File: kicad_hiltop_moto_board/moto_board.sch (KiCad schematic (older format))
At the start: 45 parts, among them J1 Conn_01x04, J2 Conn_01x03, J3 Conn_03x32_DIN41612, J4 Conn_01x03, J5 Conn_02x05_Top_Bottom, U2 LD1117S33TR_SOT223, U3 AT25DN512CSSHF-B

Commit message: Unused pind removed from moto board
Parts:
- C10, C11, C12: symbol Motor_Control_Board-rescue:C-device-Sensi_Board-rescue -> moto_board-rescue:C-device-Sensi_Board-rescue-Motor_Control_Board-rescue
- C13: symbol Motor_Control_Board-rescue:CP-device-Sensi_Board-rescue -> moto_board-rescue:CP-device-Sensi_Board-rescue-Motor_Control_Board-rescue
- D32: symbol Motor_Control_Board-rescue:D-device-Sensi_Board-rescue -> moto_board-rescue:D-device-Sensi_Board-rescue-Motor_Control_Board-rescue
- J3: symbol Motor_Control_Board-rescue:Conn_03x32_DIN41612-Devtank-Sensi_Board-rescue -> moto_board-rescue:Conn_03x32_DIN41612-Devtank-Sensi_Board-rescue-Motor_Control_Board-rescue
- JP1: symbol Motor_Control_Board-rescue:Jumper_NC_Dual-device-Sensi_Board-rescue -> moto_board-rescue:Jumper_NC_Dual-device-Sensi_Board-rescue-Motor_Control_Board-rescue
- R14, R15, R16, R17: symbol Motor_Control_Board-rescue:R-device-Sensi_Board-rescue -> moto_board-rescue:R-device-Sensi_Board-rescue-Motor_Control_Board-rescue
- TP101, TP102, TP103, TP104, TP105, TP2, TP31, TP32, TP33, TP34, TP35, TP36: symbol Motor_Control_Board-rescue:Test_Point-Connector-Sensi_Board-rescue -> moto_board-rescue:Test_Point-Connector-Sensi_Board-rescue-Motor_Control_Board-rescue
- U2: symbol Motor_Control_Board-rescue:LD1117S33TR_SOT223-regul-Sensi_Board-rescue -> moto_board-rescue:LD1117S33TR_SOT223-regul-Sensi_Board-rescue-Motor_Control_Board-rescue
- U3: symbol Motor_Control_Board-rescue:AT25_EEPROM-memory-Sensi_Board-rescue -> moto_board-rescue:AT25_EEPROM-memory-Sensi_Board-rescue-Motor_Control_Board-rescue
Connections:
- net labels removed: ADC1, ADC10, ADC11, ADC12, ADC13, ADC2, ADC3, ADC4, ADC5, ADC6, ADC7, ADC8, ADC9
- wire segments 285 -> 272
- no-connect marks 88 -> 64
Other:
- note added: "Direct PWM"
- note added: "PWM through SPI\n"

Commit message: Started on moto board layout
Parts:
- removed J2, J4: Conn_01x03, symbol Connector:Conn_01x03
- added J2, J4: Conn_01x04, Devtank_PCB_Lib:Molex2x06, symbol Connector:Conn_01x04
- added TP1, TP10, TP11, TP12, TP13, TP14, TP15, TP16, TP23, TP3, TP4, TP5, TP6, TP7, TP8, TP9: Test_Point, TestPoint:TestPoint_THTPad_D1.0mm_Drill0.5mm, symbol moto_board-rescue:Test_Point-Connector-Sensi_Board-rescue-Motor_Control_Board-r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
- J1: footprint (none) -> Connector_TE-Connectivity:TE_MATE-N-LOK_350211-1_1x04_P5.08mm_Vertical
- J5: footprint (none) -> Connector_PinHeader_2.54mm:PinHeader_2x05_P2.54mm_Vertical
- R1, R13: footprint (none) -> Resistor_SMD:R_0805_2012Metric
- R10, R11, R12, R2, R3, R4, R5, R6, R7, R8, R9: footprint (none) -> Resistor_SMD:R_0603_1608Metric
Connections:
- net 12V_EXT: now also TP12.1
- net AOUT1: now also J4.1 (Pin_1), TP13.1
- net AOUT2: now also J4.2 (Pin_2), TP14.1
- net BOUT1: now also J2.1 (Pin_1), TP15.1
- net BOUT2: now also J2.2 (Pin_2), TP16.1
- net GND: now also J2.3 (Pin_3), J4.3 (Pin_3)
- net motor_AIN1 renamed M_AIN1
- net M_AIN1: now also TP4.1
- net motor_AIN2 renamed M_AIN2
- net M_AIN2: now also TP5.1
- net motor_BIN1 renamed M_BIN1
- net M_BIN1: now also TP6.1
- net motor_BIN2 renamed M_BIN2
- net M_BIN2: now also TP7.1
- net motor_DATO renamed M_SDATO
- net M_SDATO: now also TP11.1
- net motor_FAULTn renamed M_FAULTn
- net M_FAULTn: now also TP23.1
- net motor_RESET renamed M_RESET
- net M_RESET: now also TP3.1
- net motor_SCLK renamed M_SCLK
- net M_SCLK: now also TP8.1
- net motor_SCS renamed M_SCS
- net M_SCS: now also TP10.1
- net motor_SDATI renamed M_SDATI
- net M_SDATI: now also TP9.1
- net motor_SLEEPn renamed M_SLEEPn
- net M_SLEEPn: now also TP1.1
- no-connect marks 64 -> 66

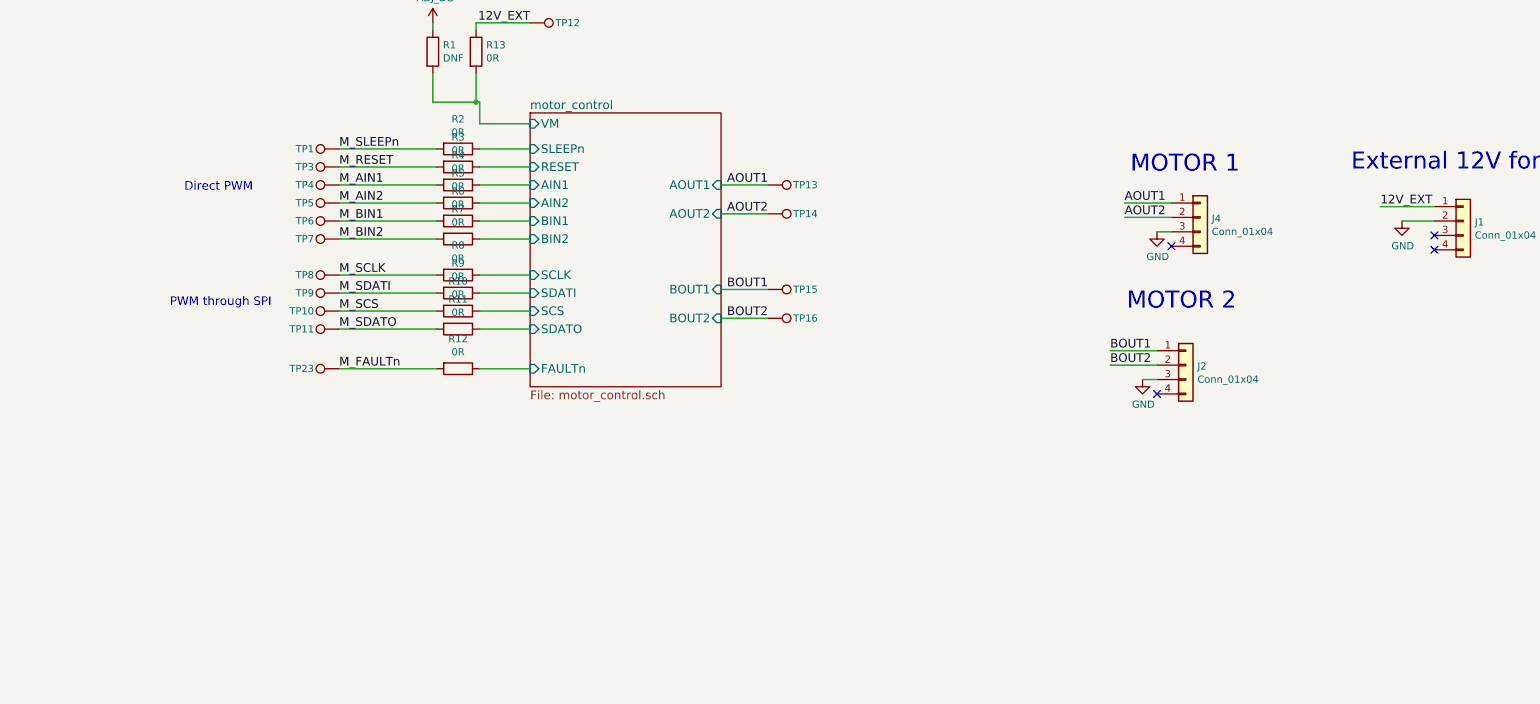
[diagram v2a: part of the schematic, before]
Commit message: Rough layout of moto board
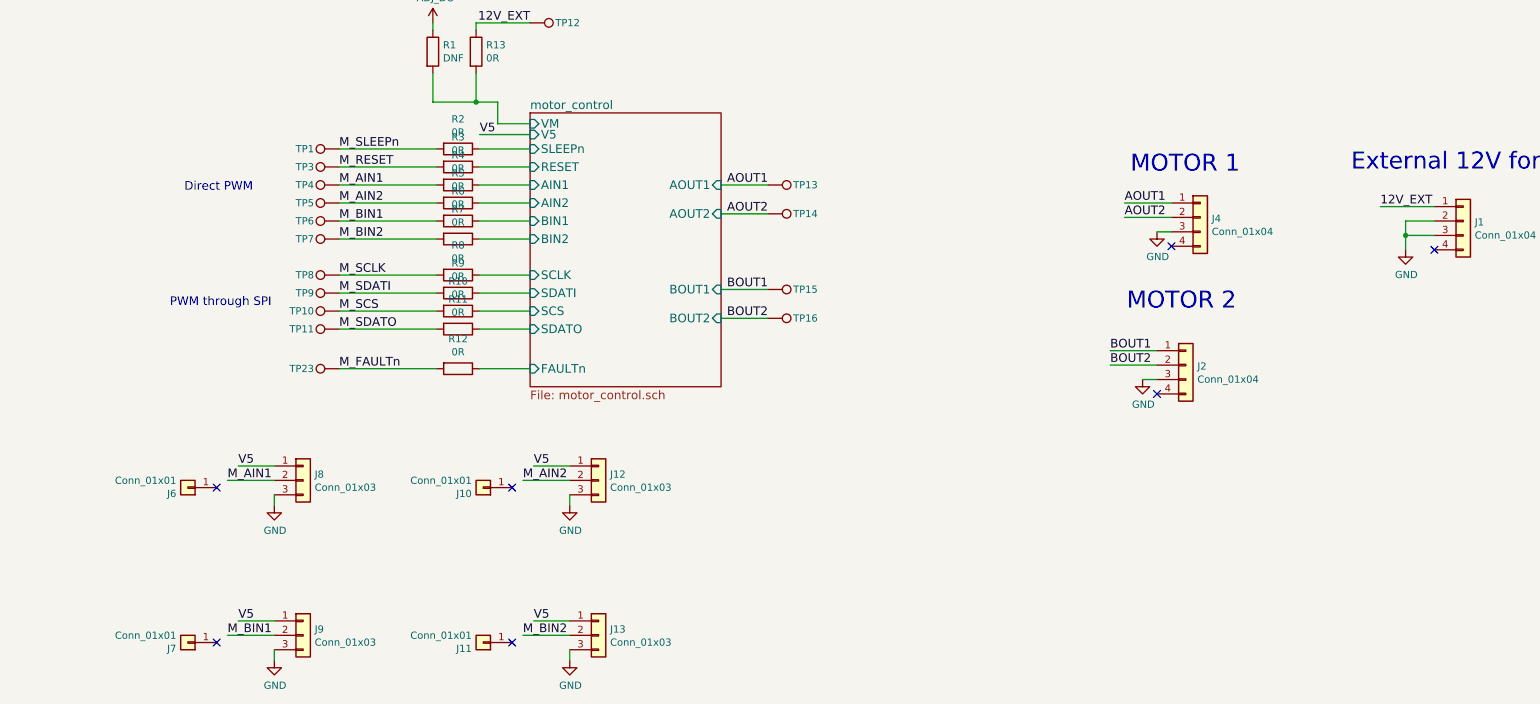
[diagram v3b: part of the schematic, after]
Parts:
- added J10, J11, J6, J7: Conn_01x01, Connector_PinHeader_2.54mm:PinHeader_1x01_P2.54mm_Vertical, symbol Connector:Conn_01x01
- added J12, J13, J8, J9: Conn_01x03, Connector_PinHeader_2.54mm:PinHeader_1x03_P2.54mm_Vertical, symbol Connector:Conn_01x03
- J2, J4: footprint Devtank_PCB_Lib:Molex2x06 -> Connector_Molex:Molex_Nano-Fit_105309-xx04_1x04_P2.50mm_Vertical
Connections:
- net GND: now also J1.3 (Pin_3), J12.3 (Pin_3), J13.3 (Pin_3), J8.3 (Pin_3), J9.3 (Pin_3)
- net M_AIN1: now also J8.2 (Pin_2)
- net M_AIN2: now also J12.2 (Pin_2)
- net M_BIN1: now also J9.2 (Pin_2)
- net M_BIN2: now also J13.2 (Pin_2)
- new net V5: J12.1 (Pin_1), J13.1 (Pin_1), J8.1 (Pin_1), J9.1 (Pin_1)
- no-connect marks 66 -> 69
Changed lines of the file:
@@
 F16 "BOUT2" I R 9025 9800 60
 F17 "VM" I L 7700 8450 60
+F18 "V5" I L 7700 8525 60
 $EndSheet
 Wire Wire Line
@@
 	7325 7800 7325 7750
 Wire Wire Line
-	7700 8450 7350 8450
-Wire Wire Line
-	7350 8450 7350 8300
+	7700 8450 7475 8450
+Wire Wire Line
+	7475 8450 7475 8300
 Wire Wire Line
 	7025 8300 7025 8100
@@
 Connection ~ 7325 8300
 Wire Wire Line
-	7325 8300 7350 8300
+	7325 8300 7475 8300
 Text Label 7700 7750 2    60   ~ 0
 12V_EXT
@@
 L power:GND #PWR04
 U 1 1 61485EFB
-P 13750 9125
-F 0 "#PWR04" H 13750 8875 50  0001 C CNN
-F 1 "GND" H 13755 8952 50  0000 C CNN
-F 2 "" H 13750 9125 50  0001 C CNN
-F 3 "" H 13750 9125 50  0001 C CNN
-	1    13750 9125
-	1    0    0    -1
-$EndComp
-NoConn ~ 13975 9225
+P 13775 9325
+F 0 "#PWR04" H 13775 9075 50  0001 C CNN
+F 1 "GND" H 13780 9152 50  0000 C CNN
+F 2 "" H 13775 9325 50  0001 C CNN
+F 3 "" H 13775 9325 50  0001 C CNN
+	1    13775 9325
+	1    0    0    -1
+$EndComp
 NoConn ~ 13975 9325
-Wire Wire Line
-	13750 9125 13975 9125
 Text Notes 15250 8975 2    118  ~ 0
 External 12V for motor\n\n
@@
 F 0 "J4" H 12430 9092 50  0000 L CNN
 F 1 "Conn_01x04" H 12430 9001 50  0000 L CNN
-F 2 "Devtank_PCB_Lib:Molex2x06" H 12350 9100 50  0001 C CNN
+F 2 "Connector_Molex:Molex_Nano-Fit_105309-xx04_1x04_P2.50mm_Vertical" H 12350 9100 50  0001 C CNN
 F 3 "~" H 12350 9100 50  0001 C CNN
 	1    12350 9100
@@
 F 0 "J2" H 12330 10117 50  0000 L CNN
 F 1 "Conn_01x04" H 12330 10026 50  0000 L CNN
-F 2 "Devtank_PCB_Lib:Molex2x06" H 12250 10125 50  0001 C CNN
+F 2 "Connector_Molex:Molex_Nano-Fit_105309-xx04_1x04_P2.50mm_Vertical" H 12250 10125 50  0001 C CNN
 F 3 "~" H 12250 10125 50  0001 C CNN
 	1    12250 10125
@@
 	0    -1   -1   0
 $EndComp
+$Comp
+L Connector:Conn_01x01 J6
+U 1 1 5DCD017F
+P 5325 10975
+F 0 "J6" H 5405 11017 50  0000 L CNN
+F 1 "Conn_01x01" H 5405 10926 50  0000 L CNN
+F 2 "Connector_PinHeader_2.54mm:PinHeader_1x01_P2.54mm_Vertical" H 5325 10975 50  0001 C CNN
+F 3 "~" H 5325 10975 50  0001 C CNN
+	1    5325 10975
+	-1   0    0    1
+$EndComp
+Wire Wire Line
+	5925 11025 5925 11100
+Wire Wire Line
+	5925 10825 5675 10825
+Wire Wire Line
+	7700 8525 7350 8525
+Text Label 7350 8525 0    60   ~ 0
+V5
+Text Label 5675 10825 0    60   ~ 0
+V5
+NoConn ~ 5525 10975
+$Comp
+L power:GND #PWR0108
+U 1 1 5DEBCBBF
+P 5925 11100
+F 0 "#PWR0108" H 5925 10850 50  0001 C CNN
+F 1 "GND" H 5930 10927 50  0000 C CNN
+F 2 "" H 5925 11100 50  0001 C CNN
+F 3 "" H 5925 11100 50  0001 C CNN
+	1    5925 11100
+	1    0    0    -1
+$EndComp
+Text Label 5600 10925 0    60   ~ 0
+M_AIN1
+Wire Wire Line
+	5600 10925 5925 10925
+$Comp
+L Connector:Conn_01x03 J8
+U 1 1 5DFB262E
+P 6125 10925
+F 0 "J8" H 6205 10967 50  0000 L CNN
+F 1 "Conn_01x03" H 6205 10876 50  0000 L CNN
+F 2 "Connector_PinHeader_2.54mm:PinHeader_1x03_P2.54mm_Vertical" H 6125 10925 50  0001 C CNN
+F 3 "~" H 6125 10925 50  0001 C CNN
+	1    6125 10925
+	1    0    0    -1
+$EndComp
+$Comp
+L Connector:Conn_01x01 J10
+U 1 1 5E06E1C9
+P 7375 10975
+F 0 "J10" H 7455 11017 50  0000 L CNN
+F 1 "Conn_01x01" H 7455 10926 50  0000 L CNN
+F 2 "Connector_PinHeader_2.54mm:PinHeader_1x01_P2.54mm_Vertical" H 7375 10975 50  0001 C CNN
+F 3 "~" H 7375 10975 50  0001 C CNN
+	1    7375 10975
+	-1   0    0    1
+$EndComp
+Wire Wire Line
+	7975 11025 7975 11100
+Wire Wire Line
+	7975 10825 7725 10825
+Text Label 7725 10825 0    60   ~ 0
+V5
+NoConn ~ 7575 10975
+$Comp
+L power:GND #PWR0109
+U 1 1 5E06E1D3
+P 7975 11100
+F 0 "#PWR0109" H 7975 10850 50  0001 C CNN
+F 1 "GND" H 7980 10927 50  0000 C CNN
+F 2 "" H 7975 11100 50  0001 C CNN
+F 3 "" H 7975 11100 50  0001 C CNN
+	1    7975 11100
+	1    0    0    -1
+$EndComp
+Text Label 7650 10925 0    60   ~ 0
+M_AIN2
+Wire Wire Line
+	7650 10925 7975 10925
+$Comp
+L Connector:Conn_01x03 J12
+U 1 1 5E06E1DB
+P 8175 10925
+F 0 "J12" H 8255 10967 50  0000 L CNN
+F 1 "Conn_01x03" H 8255 10876 50  0000 L CNN
+F 2 "Connector_PinHeader_2.54mm:PinHeader_1x03_P2.54mm_Vertical" H 8175 10925 50  0001 C CNN
+F 3 "~" H 8175 10925 50  0001 C CNN
+	1    8175 10925
+	1    0    0    -1
+$EndComp
+$Comp
+L Connector:Conn_01x01 J7
+U 1 1 5E08C189
+P 5325 12050
+F 0 "J7" H 5405 12092 50  0000 L CNN
+F 1 "Conn_01x01" H 5405 12001 50  0000 L CNN
+F 2 "Connector_PinHeader_2.54mm:PinHeader_1x01_P2.54mm_Vertical" H 5325 12050 50  0001 C CNN
+F 3 "~" H 5325 12050 50  0001 C CNN
+	1    5325 12050
+	-1   0    0    1
+$EndComp
+Wire Wire Line
+	5925 12100 5925 12175
+Wire Wire Line
+	5925 11900 5675 11900
+Text Label 5675 11900 0    60   ~ 0
+V5
+NoConn ~ 5525 12050
+$Comp
+L power:GND #PWR0110
+U 1 1 5E08C193
+P 5925 12175
+F 0 "#PWR0110" H 5925 11925 50  0001 C CNN
+F 1 "GND" H 5930 12002 50  0000 C CNN
+F 2 "" H 5925 12175 50  0001 C CNN
+F 3 "" H 5925 12175 50  0001 C CNN
+	1    5925 12175
+	1    0    0    -1
+$EndComp
+Text Label 5600 12000 0    60   ~ 0
+M_BIN1
+Wire Wire Line
+	5600 12000 5925 12000
+$Comp
+L Connector:Conn_01x03 J9
+U 1 1 5E08C19B
+P 6125 12000
+F 0 "J9" H 6205 12042 50  0000 L CNN
+F 1 "Conn_01x03" H 6205 11951 50  0000 L CNN
+F 2 "Connector_PinHeader_2.54mm:PinHeader_1x03_P2.54mm_Vertical" H 6125 12000 50  0001 C CNN
+F 3 "~" H 6125 12000 50  0001 C CNN
+	1    6125 12000
+	1    0    0    -1
+$EndComp
+$Comp
+L Connector:Conn_01x01 J11
+U 1 1 5E0AA5DC
+P 7375 12050
+F 0 "J11" H 7455 12092 50  0000 L CNN
+F 1 "Conn_01x01" H 7455 12001 50  0000 L CNN
+F 2 "Connector_PinHeader_2.54mm:PinHeader_1x01_P2.54mm_Vertical" H 7375 12050 50  0001 C CNN
+F 3 "~" H 7375 12050 50  0001 C CNN
+	1    7375 12050
+	-1   0    0    1
+$EndComp
+Wire Wire Line
+	7975 12100 7975 12175
+Wire Wire Line
+	7975 11900 7725 11900
+Text Label 7725 11900 0    60   ~ 0
+V5
+NoConn ~ 7575 12050
+$Comp
+L power:GND #PWR0111
+U 1 1 5E0AA5E6
+P 7975 12175
+F 0 "#PWR0111" H 7975 11925 50  0001 C CNN
+F 1 "GND" H 7980 12002 50  0000 C CNN
+F 2 "" H 7975 12175 50  0001 C CNN
+F 3 "" H 7975 12175 50  0001 C CNN
+	1    7975 12175
+	1    0    0    -1
+$EndComp
+Text Label 7650 12000 0    60   ~ 0
+M_BIN2
+Wire Wire Line
+	7650 12000 7975 12000
+$Comp
+L Connector:Conn_01x03 J13
+U 1 1 5E0AA5EE
+P 8175 12000
+F 0 "J13" H 8255 12042 50  0000 L CNN
+F 1 "Conn_01x03" H 8255 11951 50  0000 L CNN
+F 2 "Connector_PinHeader_2.54mm:PinHeader_1x03_P2.54mm_Vertical" H 8175 12000 50  0001 C CNN
+F 3 "~" H 8175 12000 50  0001 C CNN
+	1    8175 12000
+	1    0    0    -1
+$EndComp
+Wire Wire Line
+	13975 9125 13775 9125
+Wire Wire Line
+	13775 9125 13775 9225
+Wire Wire Line
+	13975 9225 13775 9225
+Connection ~ 13775 9225
+Wire Wire Line
+	13775 9225 13775 9325
 $EndSCHEMATC

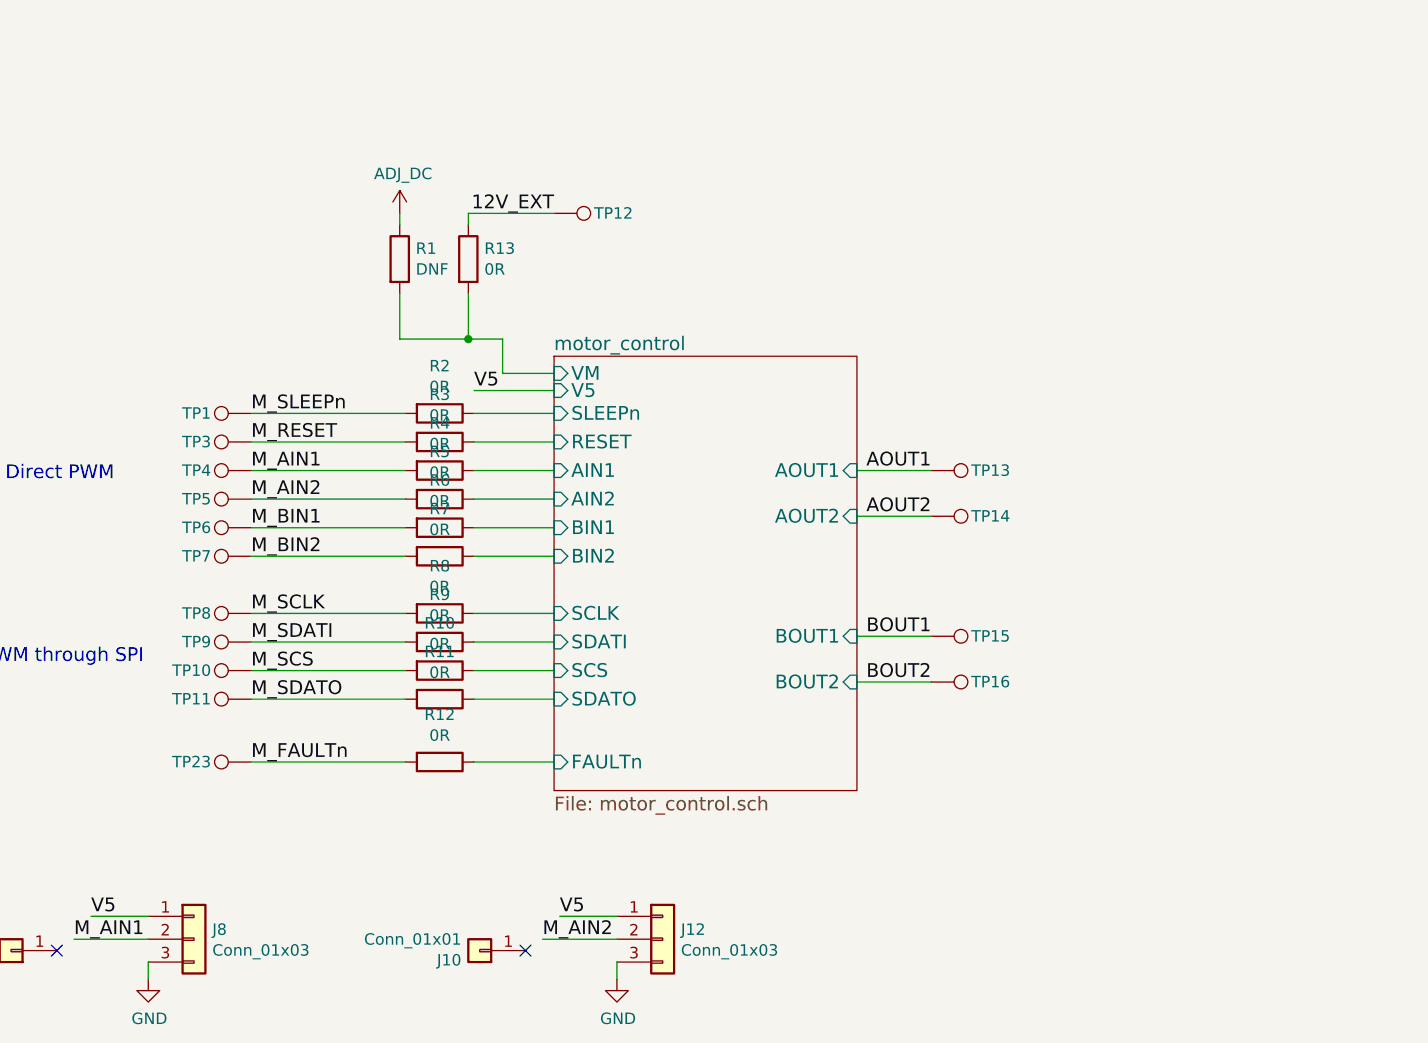
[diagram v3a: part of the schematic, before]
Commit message: Updated moto board schematic and layout
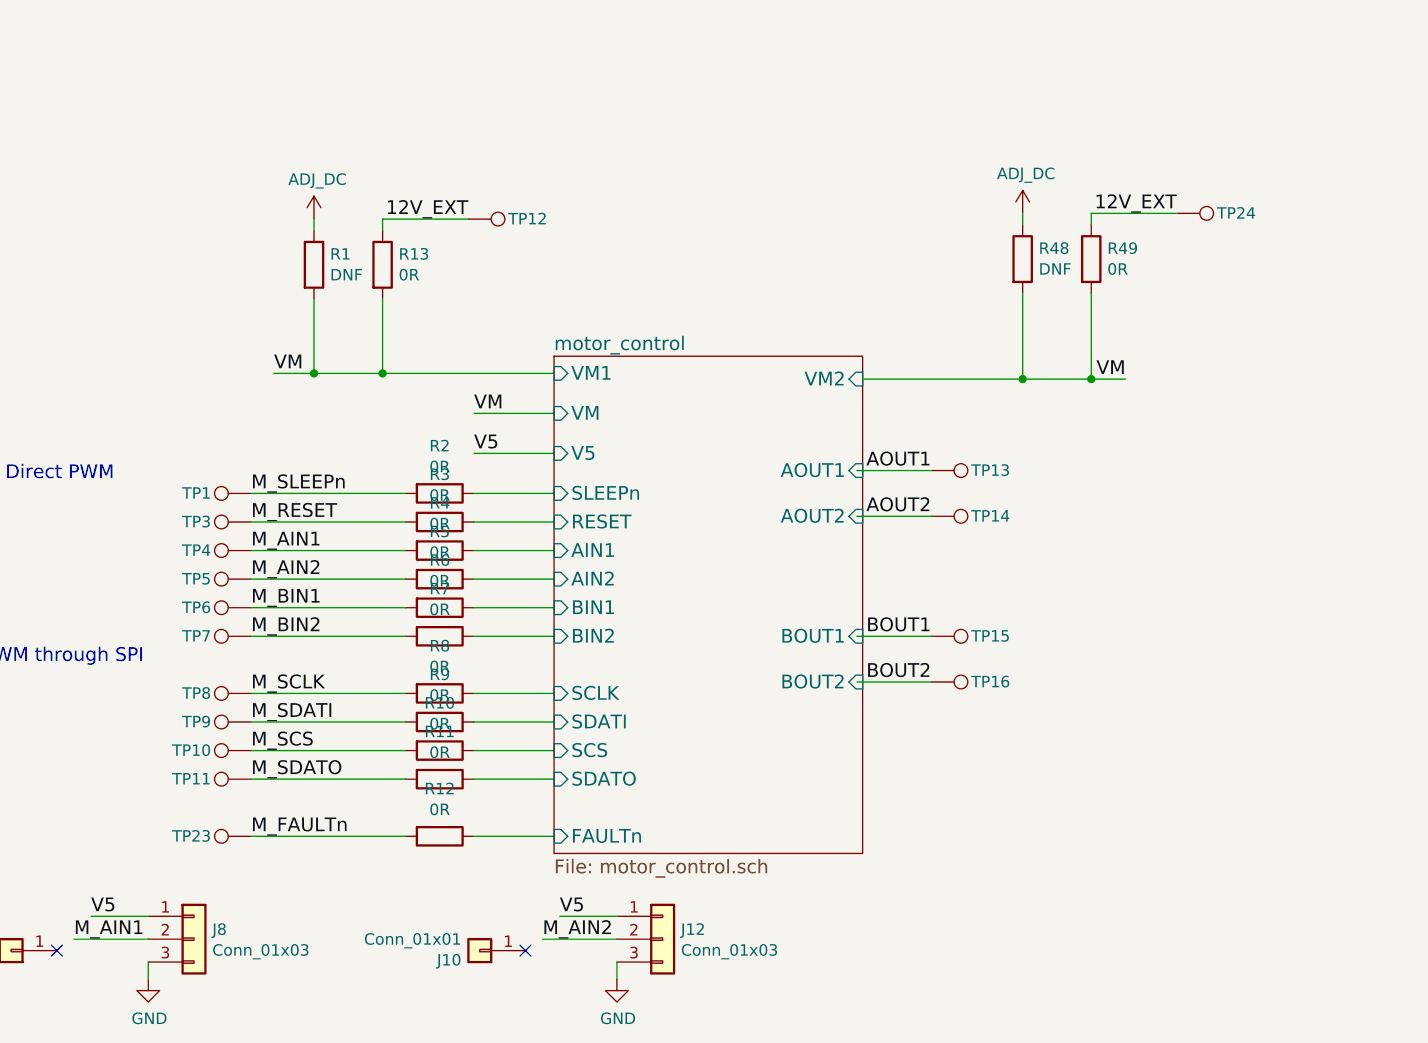
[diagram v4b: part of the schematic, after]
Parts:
- added R48: DNF, Resistor_SMD:R_0805_2012Metric, symbol device:R
- added R49: 0R, Resistor_SMD:R_0805_2012Metric, symbol device:R
- added TP24: Test_Point, TestPoint:TestPoint_THTPad_D1.0mm_Drill0.5mm, symbol moto_board-rescue:Test_Point-Connector-Sensi_Board-rescue-Motor_Control_Board-r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
- J1: footprint Connector_TE-Connectivity:TE_MATE-N-LOK_350211-1_1x04_P5.08mm_Vertical -> Devtank_PCB_Lib:Molex_8981
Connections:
- net 12V_EXT: now also R49.1, TP24.1
- net ADJ_DC: now also R48.1
- net motor_control/VM renamed VM
- net VM: now also R48.2, R49.2
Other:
- moved on the sheet: R1, R10, R11, R12, R13, R2, R3, R4, R5, R6, R7, R8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
